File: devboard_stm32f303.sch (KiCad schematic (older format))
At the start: 22 parts, among them J1 Conn_01x04, J2 USB_B_Mini, J3 Conn_01x20, J4 Conn_01x20, SW1 SW_Push, U1 STM32F303CCTx, U2 AMS1117-3.3, Y1 Crystal_Small

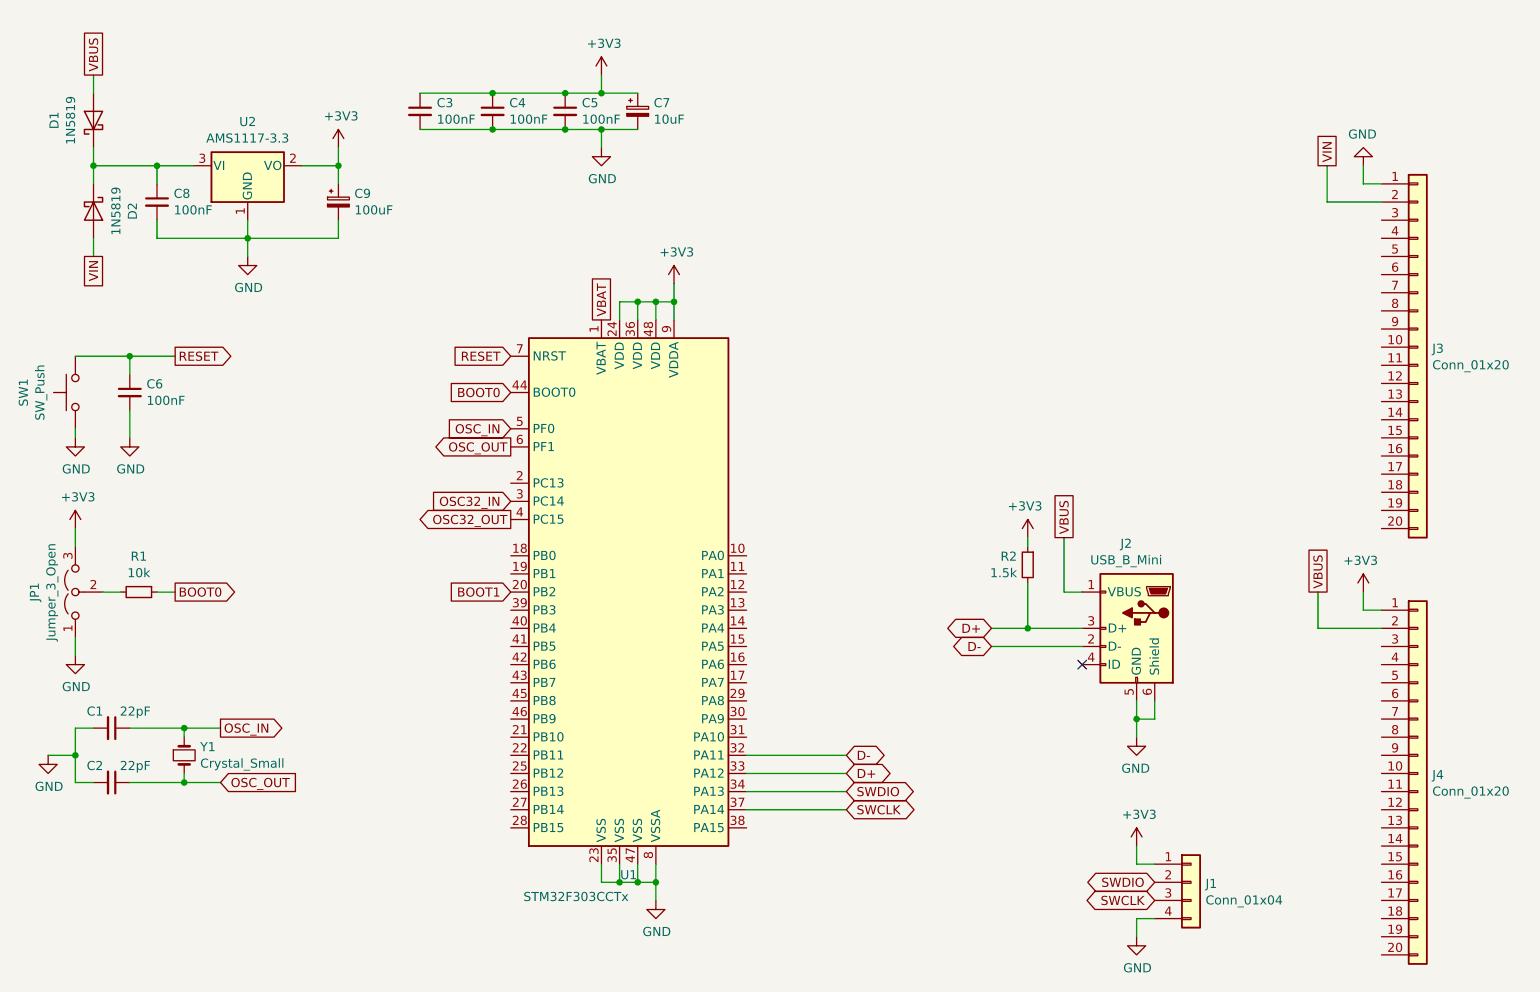
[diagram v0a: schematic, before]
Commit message: Add netlist tags
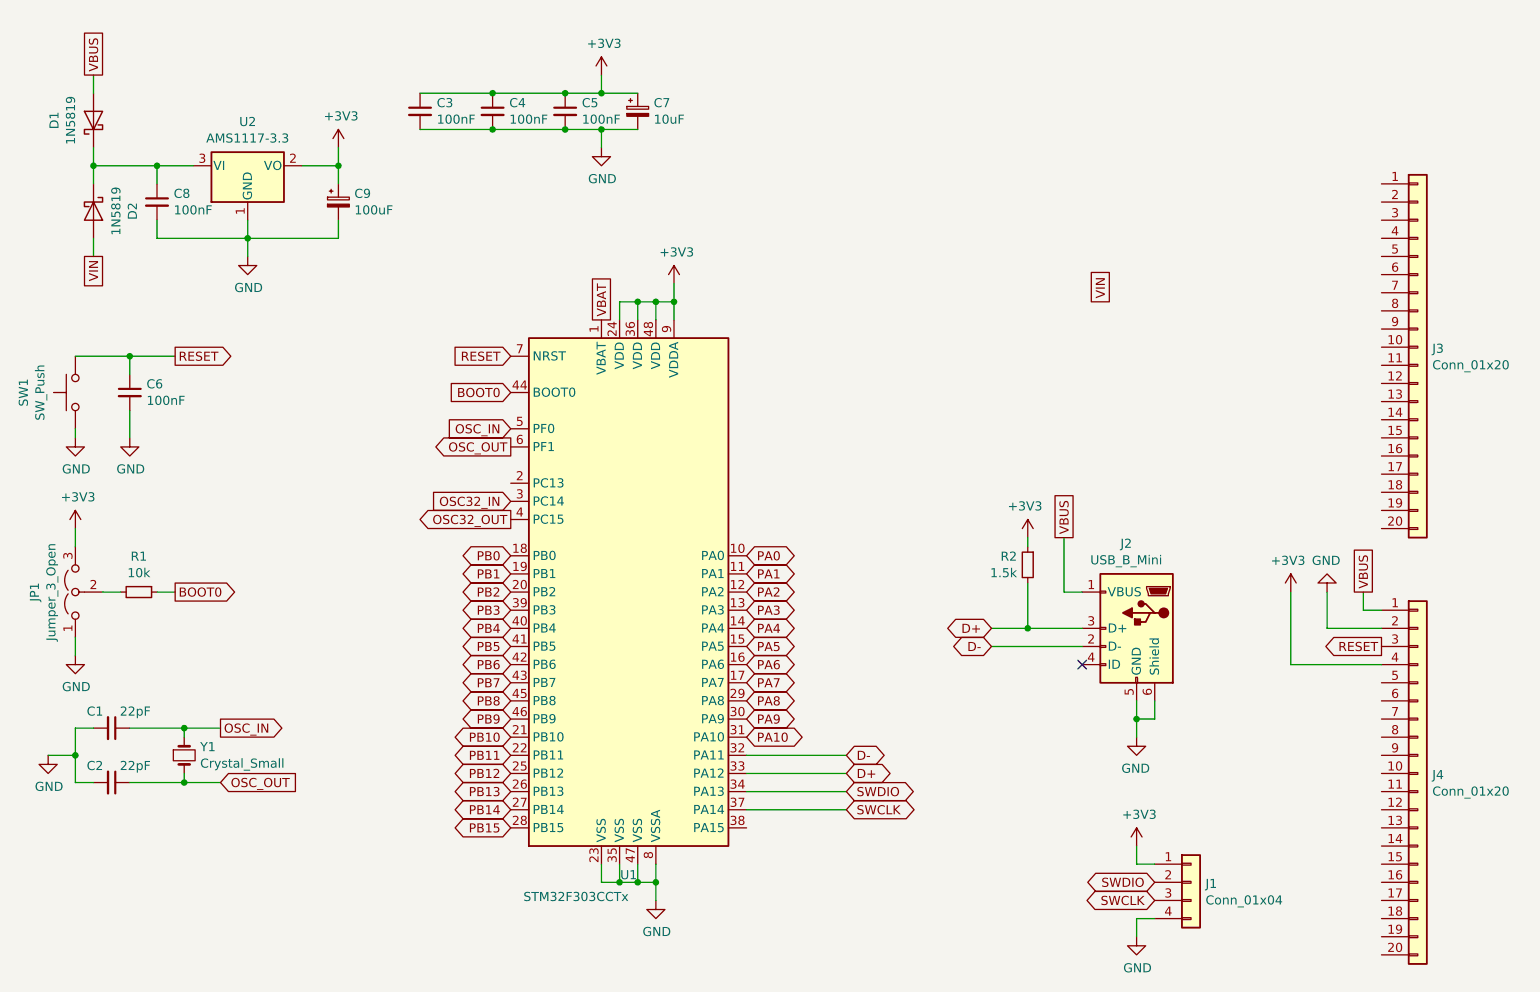
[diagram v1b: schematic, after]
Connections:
- net +3V3: now also J4.4 (Pin_4); no longer J4.1 (Pin_1)
- net GND: now also J4.2 (Pin_2); no longer J3.1 (Pin_1)
- net RESET: now also J4.3 (Pin_3)
- net VBUS: now also J4.1 (Pin_1); no longer J4.2 (Pin_2)
- net VIN: no longer J3.2 (Pin_2)
- net PA0: now reaches U1.10 (PA0)
- net PA1: now reaches U1.11 (PA1)
- net PA2: now reaches U1.12 (PA2)
- net PA3: now reaches U1.13 (PA3)
- net PA4: now reaches U1.14 (PA4)
- net PA5: now reaches U1.15 (PA5)
- net PA6: now reaches U1.16 (PA6)
- net PA7: now reaches U1.17 (PA7)
- net PB0: now reaches U1.18 (PB0)
- net PB1: now reaches U1.19 (PB1)
- net PB10: now reaches U1.21 (PB10)
- net PB11: now reaches U1.22 (PB11)
- net PB12: now reaches U1.25 (PB12)
- net PB13: now reaches U1.26 (PB13)
- net PB14: now reaches U1.27 (PB14)
- net PB15: now reaches U1.28 (PB15)
- net PA8: now reaches U1.29 (PA8)
- net PA9: now reaches U1.30 (PA9)
- net PA10: now reaches U1.31 (PA10)
- net PB3: now reaches U1.39 (PB3)
- net PB4: now reaches U1.40 (PB4)
- net PB5: now reaches U1.41 (PB5)
- net PB6: now reaches U1.42 (PB6)
- net PB7: now reaches U1.43 (PB7)
- net PB8: now reaches U1.45 (PB8)
- net PB9: now reaches U1.46 (PB9)
- net BOOT1 renamed PB2
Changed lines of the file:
@@
 Text GLabel 3850 2700 0    50   Input ~ 0
 BOOT0
-Text GLabel 3850 3800 0    50   Input ~ 0
-BOOT1
+Text GLabel 3850 3800 0    50   BiDi ~ 0
+PB2
 $Comp
 L Device:CP_Small C7
@@
 	0    1    1    0
 $EndComp
-Wire Wire Line
-	8550 1450 8550 1550
 $Comp
 L power:GND #PWR0118
 U 1 1 5E3D054A
-P 8550 1450
-F 0 "#PWR0118" H 8550 1200 50  0001 C CNN
-F 1 "GND" H 8555 1277 50  0000 C CNN
-F 2 "" H 8550 1450 50  0001 C CNN
-F 3 "" H 8550 1450 50  0001 C CNN
-	1    8550 1450
+P 8350 3800
+F 0 "#PWR0118" H 8350 3550 50  0001 C CNN
+F 1 "GND" H 8355 3627 50  0000 C CNN
+F 2 "" H 8350 3800 50  0001 C CNN
+F 3 "" H 8350 3800 50  0001 C CNN
+	1    8350 3800
 	-1   0    0    1
 $EndComp
-Wire Wire Line
-	8650 1650 8350 1650
-Wire Wire Line
-	8350 1650 8350 1450
-Wire Wire Line
-	8550 1550 8650 1550
 $Comp
 L power:+3V3 #PWR0120
 U 1 1 5E3DEE5C
-P 8550 3800
-F 0 "#PWR0120" H 8550 3650 50  0001 C CNN
-F 1 "+3V3" H 8565 3973 50  0000 C CNN
-F 2 "" H 8550 3800 50  0001 C CNN
-F 3 "" H 8550 3800 50  0001 C CNN
-	1    8550 3800
+P 8150 3800
+F 0 "#PWR0120" H 8150 3650 50  0001 C CNN
+F 1 "+3V3" H 8165 3973 50  0000 C CNN
+F 2 "" H 8150 3800 50  0001 C CNN
+F 3 "" H 8150 3800 50  0001 C CNN
+	1    8150 3800
 	-1   0    0    -1
 $EndComp
-Wire Wire Line
-	8550 3900 8650 3900
-Wire Wire Line
-	8550 3800 8550 3900
-Wire Wire Line
-	8650 4000 8300 4000
-Wire Wire Line
-	8300 4000 8300 3800
-Text GLabel 8350 1450 1    50   UnSpc ~ 0
+Text GLabel 7100 2200 1    50   UnSpc ~ 0
 VIN
 Text GLabel 1550 1950 3    50   UnSpc ~ 0
@@
 F 3 "~" H 8850 2450 50  0001 C CNN
 	1    8850 2450
-	1    0    0    -1
-$EndComp
-$Comp
-L Connector_Generic:Conn_01x20 J4
-U 1 1 5E3F1A97
-P 8850 4800
-F 0 "J4" H 8930 4792 50  0000 L CNN
-F 1 "Conn_01x20" H 8930 4701 50  0000 L CNN
-F 2 "Connector_PinHeader_2.54mm:PinHeader_1x20_P2.54mm_Vertical" H 8850 4800 50  0001 C CNN
-F 3 "~" H 8850 4800 50  0001 C CNN
-	1    8850 4800
 	1    0    0    -1
 $EndComp
@@
 Text GLabel 1550 950  1    50   UnSpc ~ 0
 VBUS
-Text GLabel 8300 3800 1    50   UnSpc ~ 0
+Text GLabel 8550 3800 1    50   UnSpc ~ 0
 VBUS
 $Comp
@@
 Wire Wire Line
 	2900 1450 2900 1550
+Wire Wire Line
+	8650 3900 8550 3900
+Wire Wire Line
+	8550 3900 8550 3800
+Wire Wire Line
+	8650 4000 8350 4000
+Wire Wire Line
+	8350 4000 8350 3800
+$Comp
+L Connector_Generic:Conn_01x20 J4
+U 1 1 5E3F1A97
+P 8850 4800
+F 0 "J4" H 8930 4792 50  0000 L CNN
+F 1 "Conn_01x20" H 8930 4701 50  0000 L CNN
+F 2 "Connector_PinHeader_2.54mm:PinHeader_1x20_P2.54mm_Vertical" H 8850 4800 50  0001 C CNN
+F 3 "~" H 8850 4800 50  0001 C CNN
+	1    8850 4800
+	1    0    0    -1
+$EndComp
+Wire Wire Line
+	8650 4200 8150 4200
+Text GLabel 8650 4100 0    50   Output ~ 0
+RESET
+Wire Wire Line
+	8150 4200 8150 3800
+Text GLabel 5150 3600 2    50   BiDi ~ 0
+PA0
+Text GLabel 5150 3700 2    50   BiDi ~ 0
+PA1
+Text GLabel 5150 3800 2    50   BiDi ~ 0
+PA2
+Text GLabel 5150 3900 2    50   BiDi ~ 0
+PA3
+Text GLabel 5150 4000 2    50   BiDi ~ 0
+PA4
+Text GLabel 5150 4100 2    50   BiDi ~ 0
+PA5
+Text GLabel 5150 4200 2    50   BiDi ~ 0
+PA6
+Text GLabel 5150 4300 2    50   BiDi ~ 0
+PA7
+Text GLabel 5150 4400 2    50   BiDi ~ 0
+PA8
+Text GLabel 5150 4500 2    50   BiDi ~ 0
+PA9
+Text GLabel 5150 4600 2    50   BiDi ~ 0
+PA10
+Text GLabel 3850 3600 0    50   BiDi ~ 0
+PB0
+Text GLabel 3850 3700 0    50   BiDi ~ 0
+PB1
+Text GLabel 3850 4100 0    50   BiDi ~ 0
+PB5
+Text GLabel 3850 3900 0    50   BiDi ~ 0
+PB3
+Text GLabel 3850 4000 0    50   BiDi ~ 0
+PB4
+Text GLabel 3850 4400 0    50   BiDi ~ 0
+PB8
+Text GLabel 3850 4700 0    50   BiDi ~ 0
+PB11
+Text GLabel 3850 4500 0    50   BiDi ~ 0
+PB9
+Text GLabel 3850 4600 0    50   BiDi ~ 0
+PB10
+Text GLabel 3850 5000 0    50   BiDi ~ 0
+PB14
+Text GLabel 3850 4800 0    50   BiDi ~ 0
+PB12
+Text GLabel 3850 4900 0    50   BiDi ~ 0
+PB13
+Text GLabel 3850 5100 0    50   BiDi ~ 0
+PB15
+Text GLabel 3850 4200 0    50   BiDi ~ 0
+PB6
+Text GLabel 3850 4300 0    50   BiDi ~ 0
+PB7
 $EndSCHEMATC

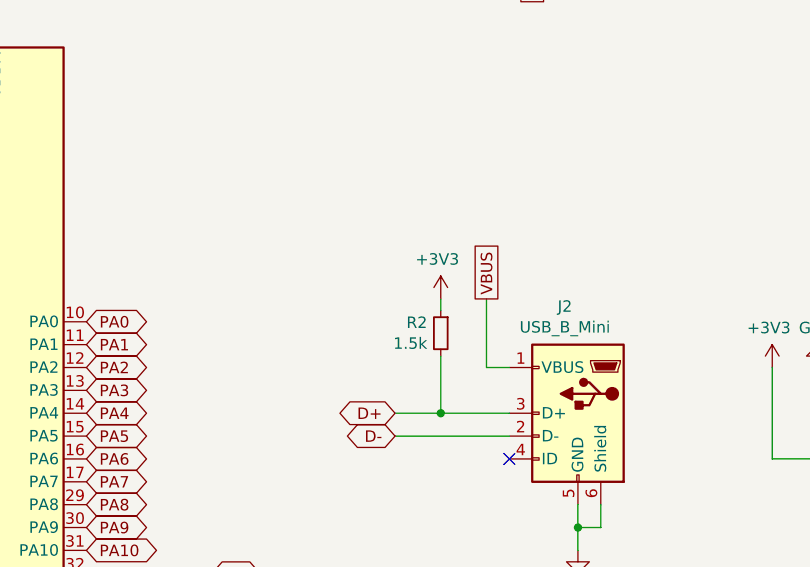
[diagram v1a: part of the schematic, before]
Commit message: Add polyfuse
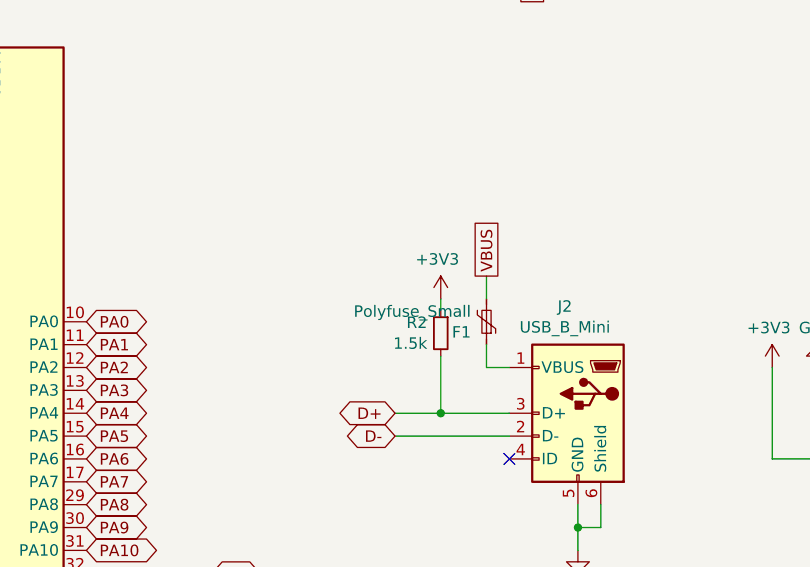
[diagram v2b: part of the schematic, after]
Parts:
- added F1: Polyfuse_Small, Fuse:Fuse_1206_3216Metric, symbol Device:Polyfuse_Small
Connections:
- net VBUS: now also F1.2; no longer J2.1 (VBUS)
- new net: F1.1, J2.1 (VBUS)
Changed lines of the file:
@@
 	7000 3800 6900 3800
 Wire Wire Line
-	6900 3800 6900 3500
+	6900 3800 6900 3700
 Wire Wire Line
 	7300 4400 7300 4500
@@
 Wire Wire Line
 	1550 1050 1550 950
-Text GLabel 6900 3500 1    50   UnSpc ~ 0
-VBUS
 Text GLabel 1550 950  1    50   UnSpc ~ 0
 VBUS
@@
 Text GLabel 3850 4300 0    50   BiDi ~ 0
 PB7
+$Comp
+L Device:Polyfuse_Small F1
+U 1 1 5E3ACE76
+P 6900 3600
+F 0 "F1" H 6968 3646 50  0000 L CNN
+F 1 "Polyfuse_Small" H 6968 3555 50  0000 L CNN
+F 2 "Fuse:Fuse_1206_3216Metric" H 6950 3400 50  0001 L CNN
+F 3 "~" H 6900 3600 50  0001 C CNN
+	1    6900 3600
+	-1   0    0    1
+$EndComp
+Text GLabel 6900 3400 1    50   UnSpc ~ 0
+VBUS
+Wire Wire Line
+	6900 3400 6900 3500
 $EndSCHEMATC

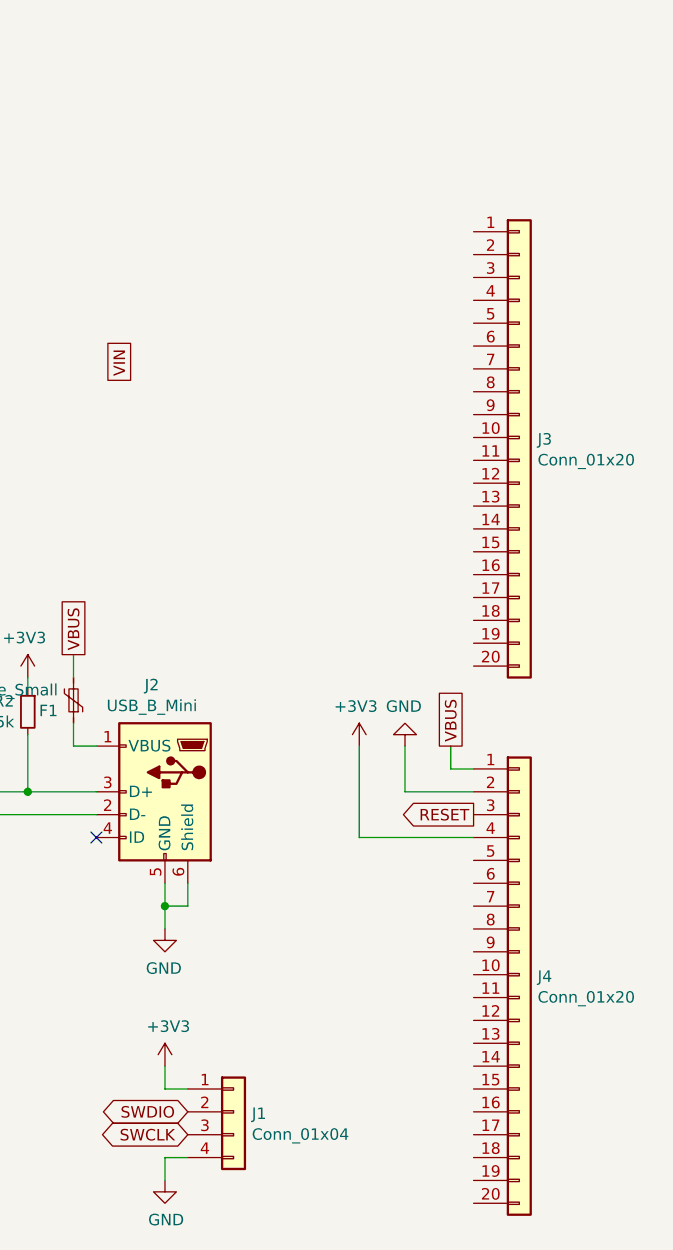
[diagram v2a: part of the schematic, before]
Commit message: Add promicro pinout schematic
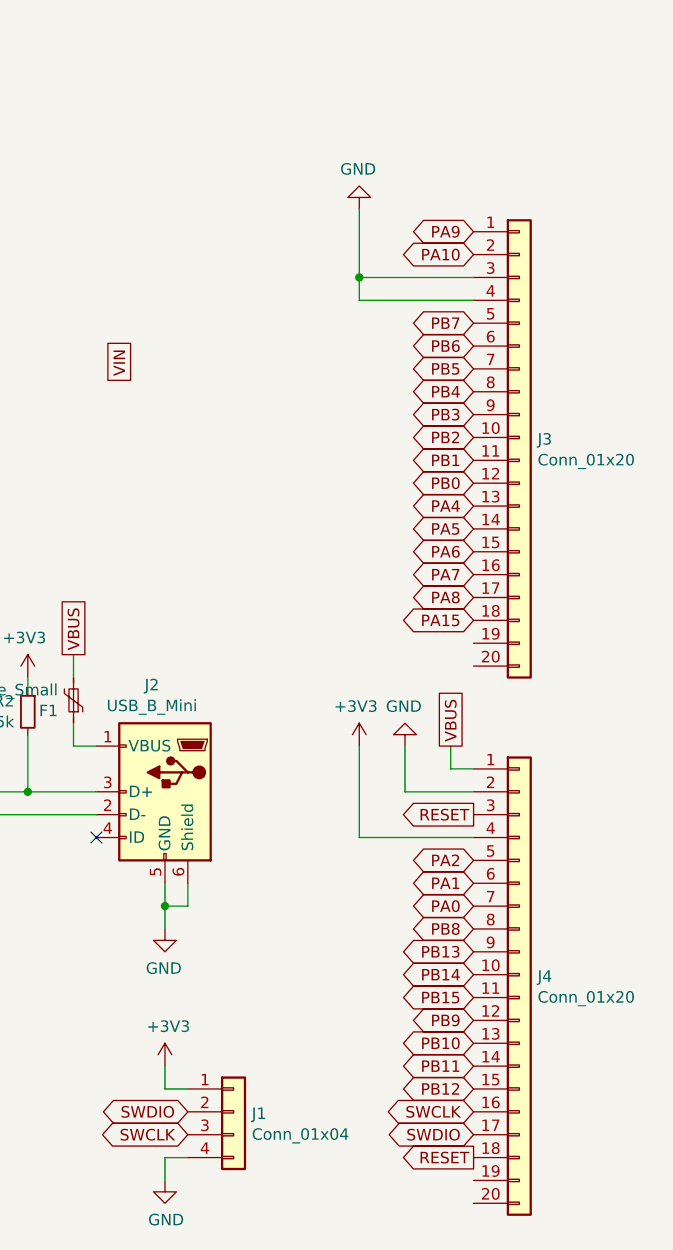
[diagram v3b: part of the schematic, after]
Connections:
- net GND: now also J3.3 (Pin_3), J3.4 (Pin_4)
- net PA0: now also J4.7 (Pin_7)
- net PA1: now also J4.6 (Pin_6)
- net PA10: now also J3.2 (Pin_2)
- net PA2: now also J4.5 (Pin_5)
- net PA4: now also J3.13 (Pin_13)
- net PA5: now also J3.14 (Pin_14)
- net PA6: now also J3.15 (Pin_15)
- net PA7: now also J3.16 (Pin_16)
- net PA8: now also J3.17 (Pin_17)
- net PA9: now also J3.1 (Pin_1)
- net PB0: now also J3.12 (Pin_12)
- net PB1: now also J3.11 (Pin_11)
- net PB10: now also J4.13 (Pin_13)
- net PB11: now also J4.14 (Pin_14)
- net PB12: now also J4.15 (Pin_15)
- net PB13: now also J4.9 (Pin_9)
- net PB14: now also J4.10 (Pin_10)
- net PB15: now also J4.11 (Pin_11)
- net PB2: now also J3.10 (Pin_10)
- net PB3: now also J3.9 (Pin_9)
- net PB4: now also J3.8 (Pin_8)
- net PB5: now also J3.7 (Pin_7)
- net PB6: now also J3.6 (Pin_6)
- net PB7: now also J3.5 (Pin_5)
- net PB8: now also J4.8 (Pin_8)
- net PB9: now also J4.12 (Pin_12)
- net RESET: now also J4.18 (Pin_18)
- net SWCLK: now also J4.16 (Pin_16)
- net SWDIO: now also J4.17 (Pin_17)
- net PA15: now reaches J3.18 (Pin_18)
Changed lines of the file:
@@
 Wire Wire Line
 	6900 3400 6900 3500
+Text GLabel 8650 4300 0    50   BiDi ~ 0
+PA2
+Text GLabel 8650 4400 0    50   BiDi ~ 0
+PA1
+Text GLabel 8650 4500 0    50   BiDi ~ 0
+PA0
+Text GLabel 8650 4600 0    50   BiDi ~ 0
+PB8
+Text GLabel 8650 4700 0    50   BiDi ~ 0
+PB13
+Text GLabel 8650 4800 0    50   BiDi ~ 0
+PB14
+Text GLabel 8650 4900 0    50   BiDi ~ 0
+PB15
+Text GLabel 8650 5000 0    50   BiDi ~ 0
+PB9
+Text GLabel 8650 5100 0    50   BiDi ~ 0
+PB10
+Text GLabel 8650 5200 0    50   BiDi ~ 0
+PB11
+Text GLabel 8650 5300 0    50   BiDi ~ 0
+PB12
+Text GLabel 8650 5400 0    50   BiDi ~ 0
+SWCLK
+Text GLabel 8650 5500 0    50   BiDi ~ 0
+SWDIO
+Text GLabel 8650 5600 0    50   Output ~ 0
+RESET
+Text GLabel 8650 1550 0    50   BiDi ~ 0
+PA9
+Text GLabel 8650 1650 0    50   BiDi ~ 0
+PA10
+$Comp
+L power:GND #PWR?
+U 1 1 5E3772DF
+P 8150 1450
+F 0 "#PWR?" H 8150 1200 50  0001 C CNN
+F 1 "GND" H 8155 1277 50  0000 C CNN
+F 2 "" H 8150 1450 50  0001 C CNN
+F 3 "" H 8150 1450 50  0001 C CNN
+	1    8150 1450
+	-1   0    0    1
+$EndComp
+Wire Wire Line
+	8650 1850 8150 1850
+Wire Wire Line
+	8650 1750 8150 1750
+Wire Wire Line
+	8150 1450 8150 1750
+Connection ~ 8150 1750
+Wire Wire Line
+	8150 1750 8150 1850
+Text GLabel 8650 1950 0    50   BiDi ~ 0
+PB7
+Text GLabel 8650 2050 0    50   BiDi ~ 0
+PB6
+Text GLabel 8650 2150 0    50   BiDi ~ 0
+PB5
+Text GLabel 8650 2250 0    50   BiDi ~ 0
+PB4
+Text GLabel 8650 2350 0    50   BiDi ~ 0
+PB3
+Text GLabel 8650 2450 0    50   BiDi ~ 0
+PB2
+Text GLabel 8650 2550 0    50   BiDi ~ 0
+PB1
+Text GLabel 8650 2650 0    50   BiDi ~ 0
+PB0
+Text GLabel 8650 2750 0    50   BiDi ~ 0
+PA4
+Text GLabel 8650 2850 0    50   BiDi ~ 0
+PA5
+Text GLabel 8650 2950 0    50   BiDi ~ 0
+PA6
+Text GLabel 8650 3050 0    50   BiDi ~ 0
+PA7
+Text GLabel 8650 3150 0    50   BiDi ~ 0
+PA8
+Text GLabel 8650 3250 0    50   BiDi ~ 0
+PA15
 $EndSCHEMATC
